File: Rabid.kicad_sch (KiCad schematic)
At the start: 222 parts, among them J1 USB Header, SW1 Esc, SW10 A, SW100 Unused, SW101 Unused, SW102 →, SW11 Z, SW12 LMeta, SW13 F1, SW14 2, SW15 W, SW16 S, SW17 X, SW18 LAlt, SW19 F2, SW2 Tilde, SW20 3, SW21 E, SW22 D, SW23 C, SW24 Unused, SW25 F3, SW26 4, SW27 R, SW28 F, SW29 V, SW3 Tab, SW30 Unused, SW31 F4, SW32 5, SW33 T, SW34 G, SW35 B, SW36 Unused, SW37 F5, SW38 6, SW39 Y, SW4 CapsLk, SW40 H, SW41 N, SW42 Space, SW43 F6, SW44 7, SW45 U, SW46 J, SW47 M, SW48 Unused, SW49 F7, SW5 LShift, SW50 8, SW51 I, SW52 K, SW53 ,, SW54 Unused, SW55 F8, SW56 9, SW57 O, SW58 L, SW59 ., SW6 LCtrl, SW60 Unused, SW61 F9, SW62 0, SW63 P, SW64 ;, SW65 /, SW66 AltGr, SW67 F10, SW68 -, SW69 [, SW7 Unused, SW70 ", SW71 RShift, SW72 RMeta, SW73 F11, SW74 =, SW75 ], SW76 ↲, SW77 Unused, SW78 Fn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

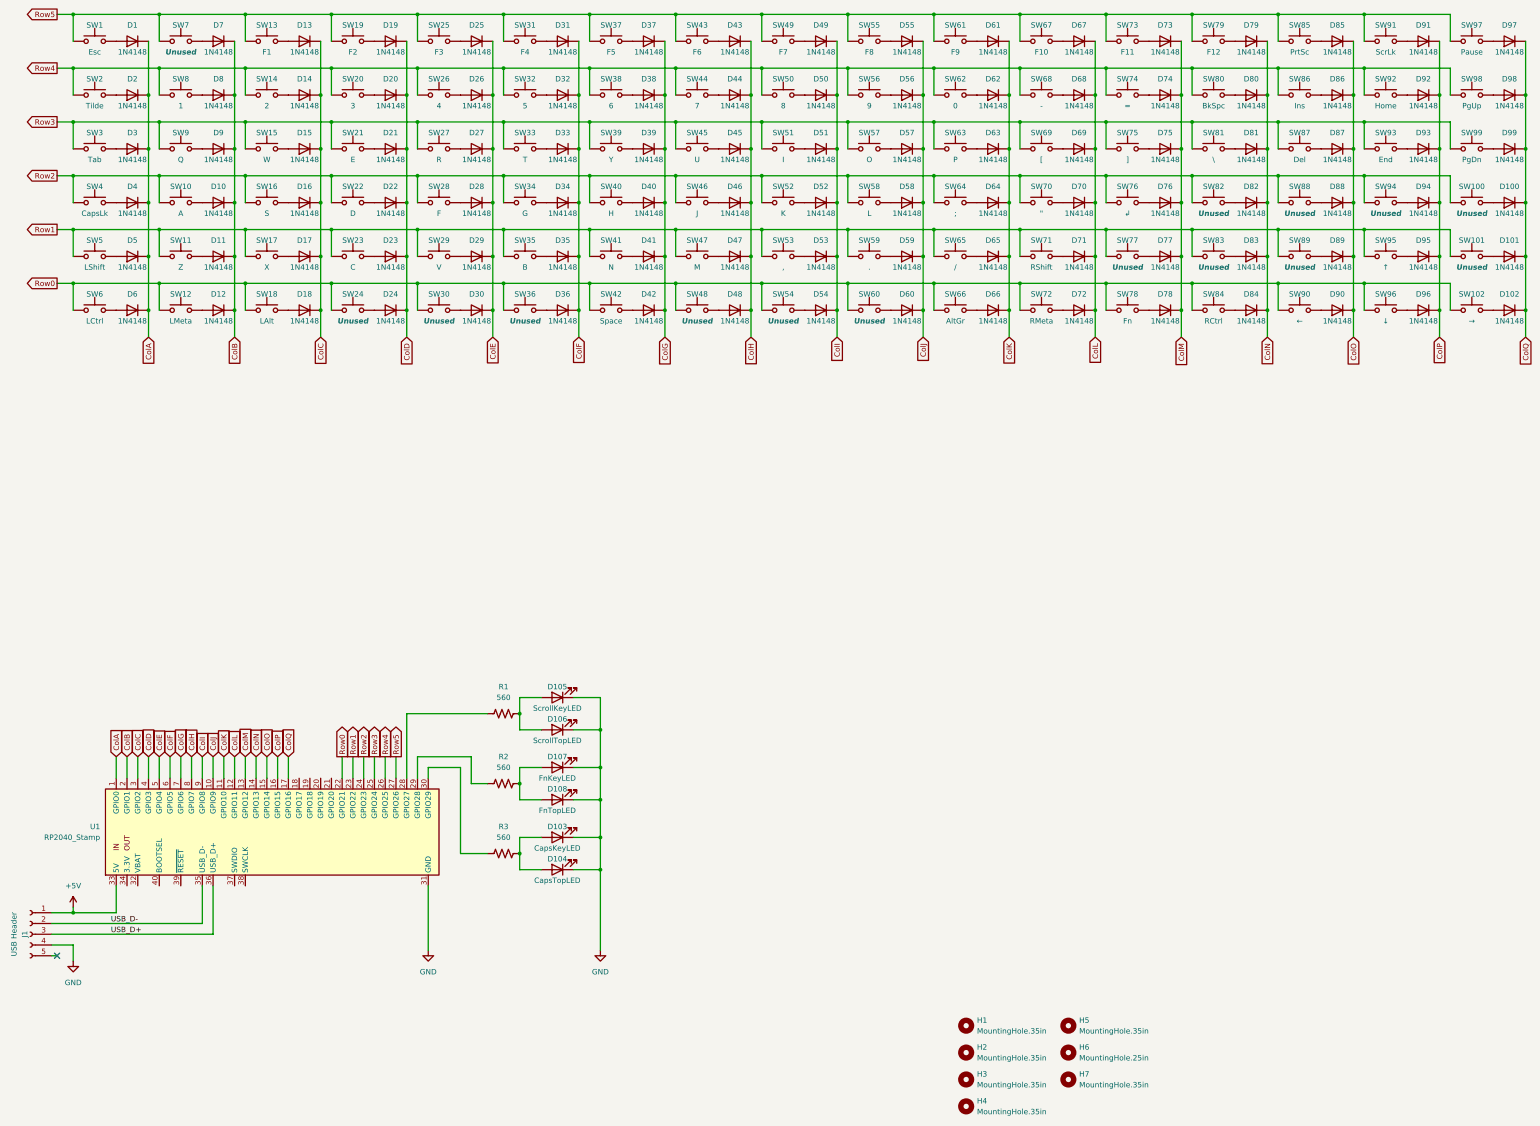
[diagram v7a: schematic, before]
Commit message: Create a separate footprint for MX switches with LED.
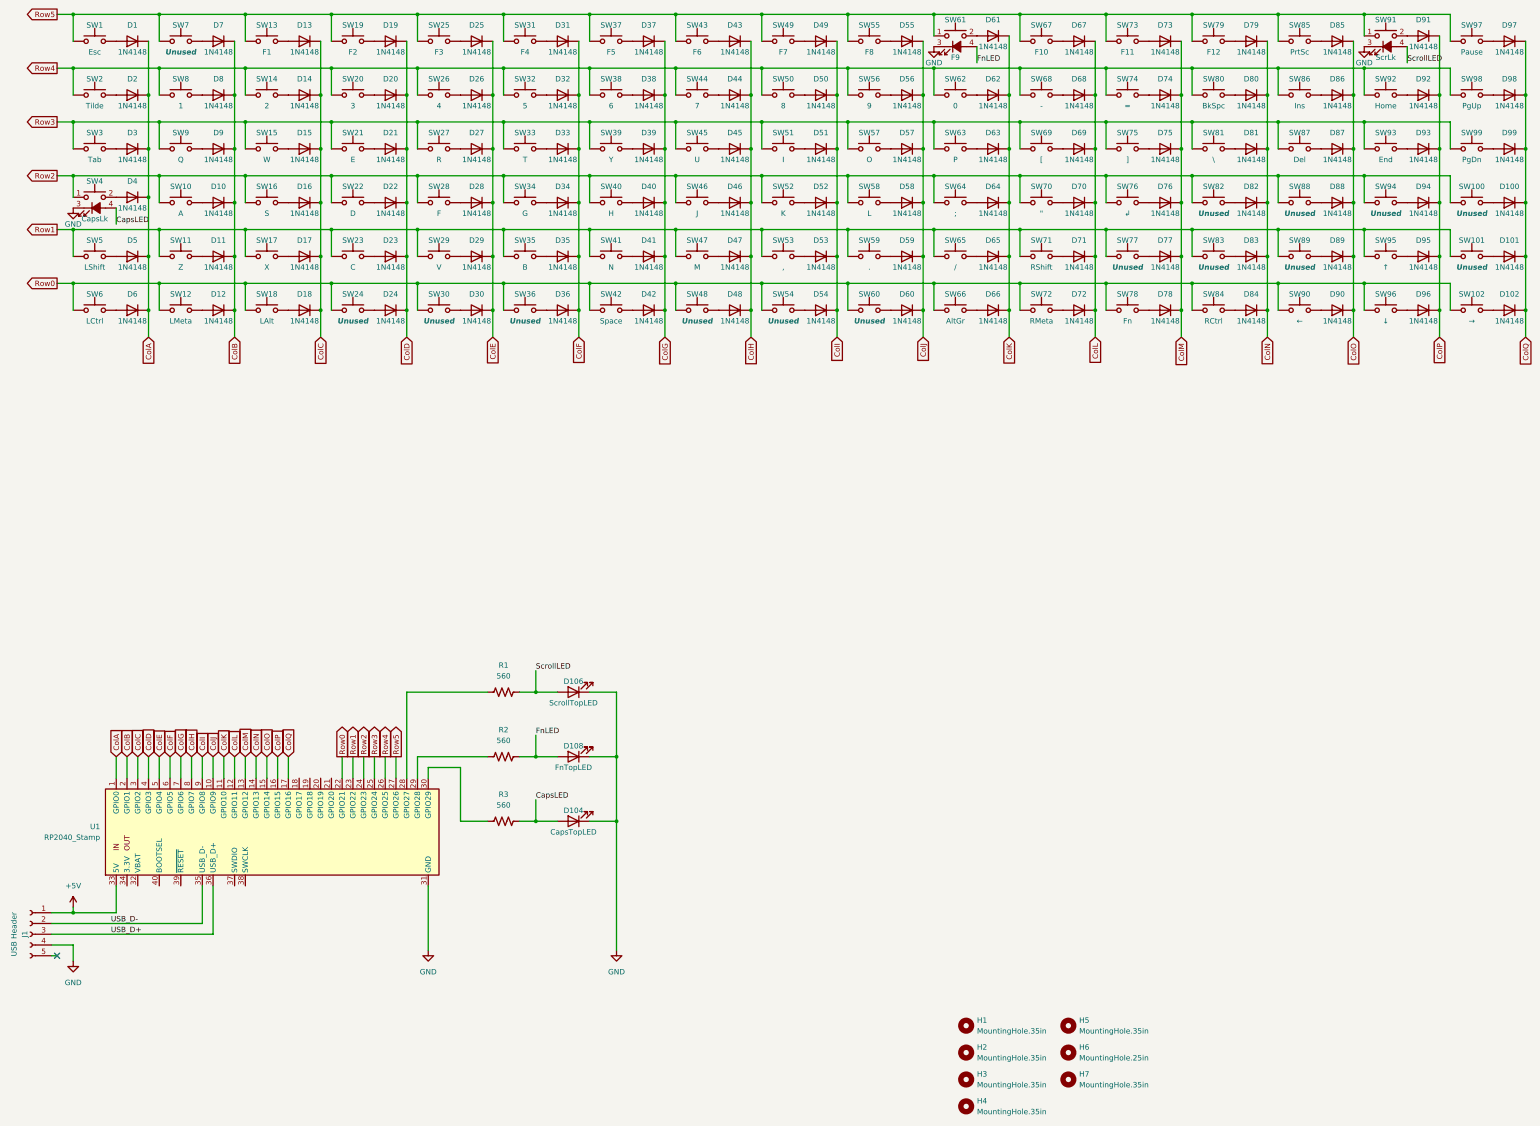
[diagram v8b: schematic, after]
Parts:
- removed D103: CapsKeyLED, LED_THT:LED_D3.0mm, symbol Device:LED
- removed D105: ScrollKeyLED, LED_THT:LED_D3.0mm, symbol Device:LED
- removed D107: FnKeyLED, LED_THT:LED_D3.0mm, symbol Device:LED
- H1, H2, H3, H4, H5, H7: footprint MountingHole:MountingHole_4.3mm_M4 -> RabidKeyboard:MountingHole_.35in
- H6: footprint MountingHole:MountingHole_4.3mm_M4 -> RabidKeyboard:MountingHole_.25in
- SW4: footprint Button_Switch_Keyboard:SW_Cherry_MX_1.75u_PCB -> RabidKeyboard:SW_Cherry_MX_1.75u_PCB_LED; symbol Switch:SW_Push -> Switch:SW_Push_LED
- SW61, SW91: footprint RabidKeyboard:SW_Cherry_MX_1.00u_PCB -> RabidKeyboard:SW_Cherry_MX_1.00u_PCB_LED; symbol Switch:SW_Push -> Switch:SW_Push_LED
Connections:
- net GND: now also SW4.3 (K), SW61.3 (K), SW91.3 (K)
- net CapsLED: now reaches D104.2 (A), R3.2
- net CapsLED: now also SW4.4 (A)
- net FnLED: now reaches D108.2 (A), R2.2
- net FnLED: now also SW61.4 (A)
- net ScrollLED: now reaches D106.2 (A), R1.2
- net ScrollLED: now also SW91.4 (A)
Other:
- moved on the sheet: D104, D106, D108, D4, D61, D91, R1, R2, R3
